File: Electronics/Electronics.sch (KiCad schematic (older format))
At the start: 40 parts

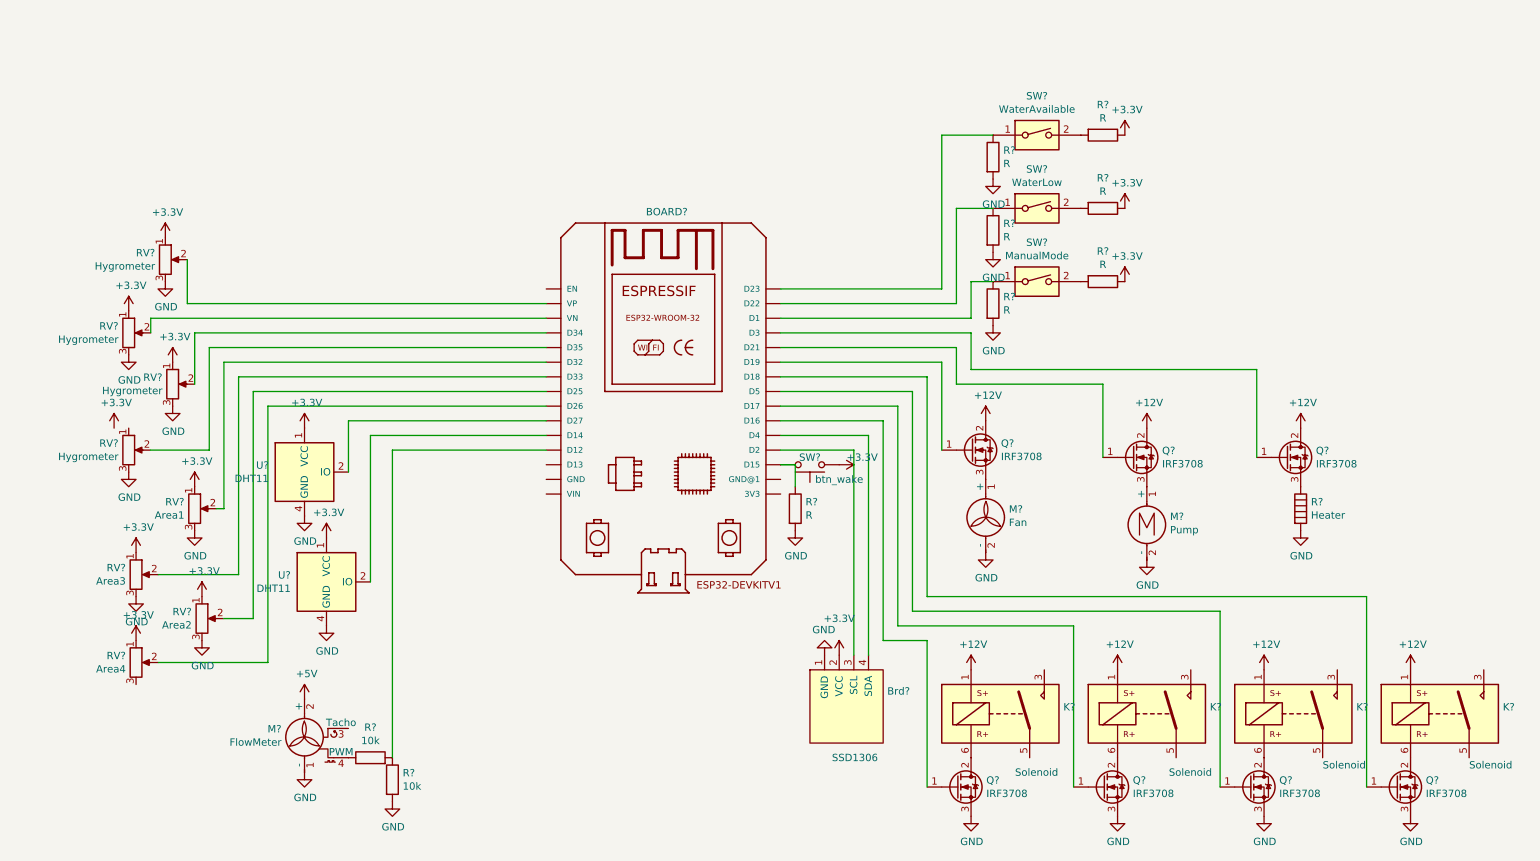
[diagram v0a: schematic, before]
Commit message: annotations and added regulator to electronics
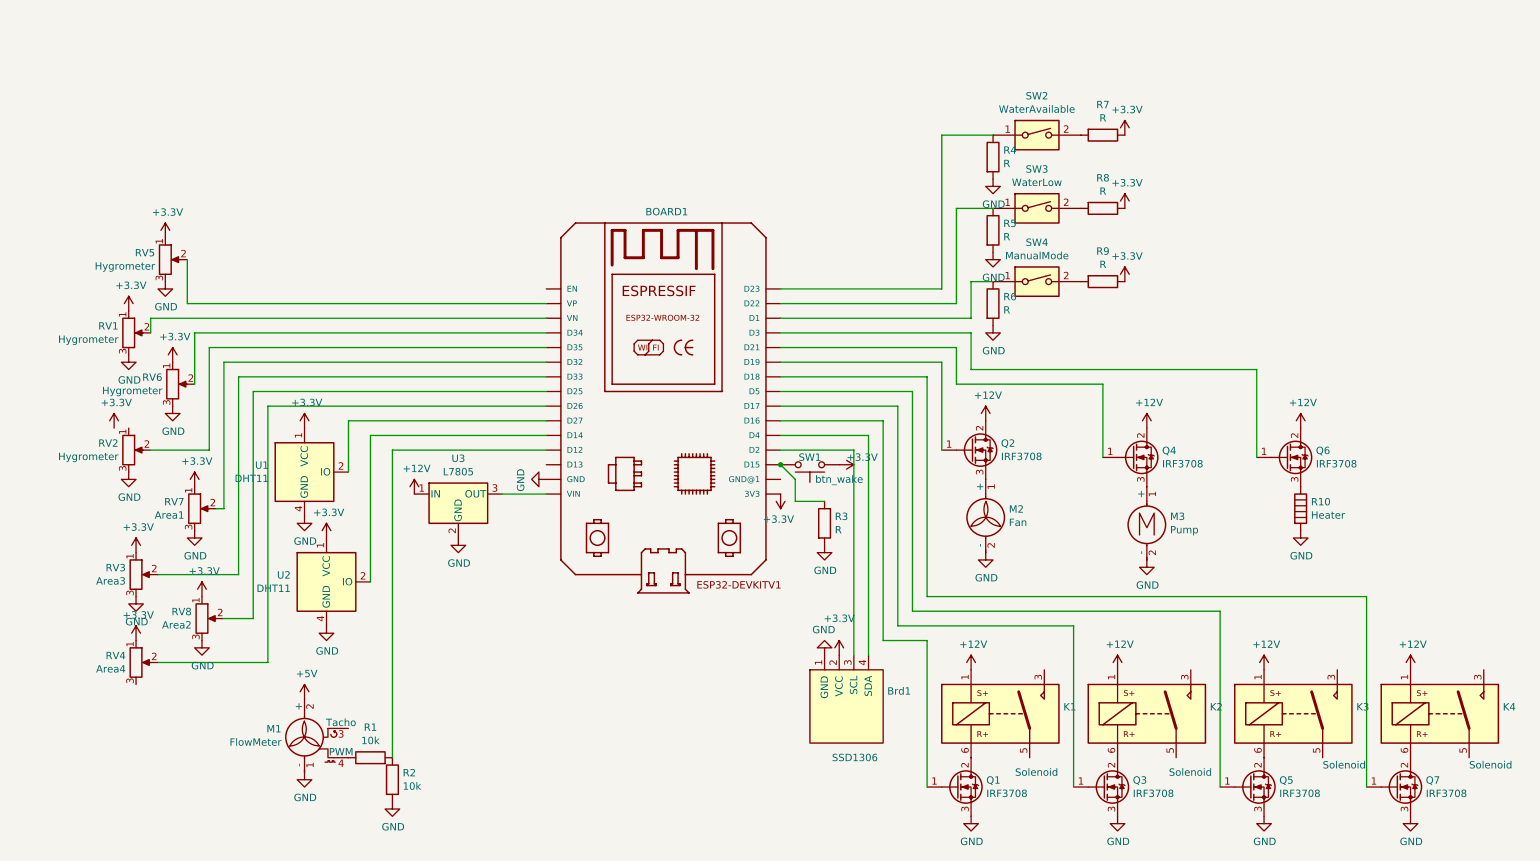
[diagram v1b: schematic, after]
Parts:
- added U3: L7805, symbol Regulator_Linear:L7805
- gave numbers to parts that had none: 40
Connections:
- net +12V: now also U3.1 (IN)
- net +3V3: now also BOARD1.3V3
- net GND: now also BOARD1.GND, U3.2 (GND)
- net at BOARD1.VIN: now also U3.3 (OUT)
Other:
- moved on the sheet: R3

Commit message: added photos and readme, updated electronics
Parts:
- removed U1, U2: DHT11, Sensor:Aosong_DHT11_5.5x12.0_P2.54mm, symbol Sensor:DHT11
- added BT1: Battery_Cell, symbol Device:Battery_Cell
- added SC1: Solar_Cell, symbol Device:Solar_Cell
- added U1: SolarChargeController, symbol Electronics-rescue:SolarChargeController-Electronics-cache
- added U2: HTU31D, symbol Electronics-cache:HTU31D
- added U?: DS3231M, Package_SO:SOIC-16W_7.5x10.3mm_P1.27mm, symbol Timer_RTC:DS3231M
- added U?: L78S05, symbol Electronics-rescue:L7805-Regulator_Linear
- K1, K2, K3, K4: symbol Relay:ADW11 -> Electronics-rescue:ADW11-Relay
- M1: symbol Motor:Fan_Tacho_PWM -> Electronics-rescue:Fan_Tacho_PWM-Motor
- M2: symbol Motor:Fan -> Electronics-rescue:Fan-Motor
- M3: symbol Motor:Motor_DC -> Electronics-rescue:Motor_DC-Motor
- Q1, Q2, Q3, Q4, Q5, Q6, Q7: symbol Transistor_FET:IRLB8721PBF -> Electronics-rescue:IRLB8721PBF-Transistor_FET
- R1, R2, R3, R4, R5, R6, R7, R8, R9: symbol Device:R -> Electronics-rescue:R-Device
- R10: symbol Device:Heater -> Electronics-rescue:Heater-Device
- RV1, RV2, RV3, RV4, RV5, RV6, RV7, RV8: symbol Device:R_POT -> Electronics-rescue:R_POT-Device
- SW1: symbol Switch:SW_Push -> Electronics-rescue:SW_Push-Switch
- SW2, SW3, SW4: symbol Switch:SW_DIP_x01 -> Electronics-rescue:SW_DIP_x01-Switch
- U3: value L7805 -> L78S33; symbol Regulator_Linear:L7805 -> Electronics-rescue:L7805-Regulator_Linear
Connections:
- net +12V: now also U1.~ (Solar-), U?.1 (IN)
- net +3V3: now also RV2.1, U3.3 (OUT), U2.~ (VCC), U?.2 (VCC)
- net +5V: now also BOARD1.VIN, U?.3 (OUT)
- net GND: now also U1.~ (Solar-), U2.~ (VCC), U?.10 (GND), U?.11 (GND), U?.12 (GND), U?.13 (GND), U?.2 (GND), U?.5 (GND), U?.6 (GND), U?.7 (GND), U?.8 (GND), U?.9 (GND)
- net at BOARD1.D2, Brd1.3 (SCL): now also U2.~ (VCC), U?.16 (SCL)
- net at BOARD1.D4, Brd1.4 (SDA): now also U2.~ (VCC), U?.15 (SDA)
- net at M1.3 (PWM): now also R1.1
- new net: SC1.1 (+), U1.~ (Solar-)
- new net: SC1.2 (-), U1.~ (Solar-)
- new net: BT1.1 (+), U1.~ (Solar-)
- new net: BT1.2 (-), U1.~ (Solar-)
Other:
- note added: "Display"
- note added: "Real Time Clock"
- note added: "Temperature & \nHumidity\nSensor"
- moved on the sheet: U3
